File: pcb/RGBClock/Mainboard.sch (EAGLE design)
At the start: 88 parts, among them IC1 MCP23017SO, K1 G6K-2F, K2 G6K-2F, K3 G6K-2F, K4 G6K-2F, U1 71918-126LF, U10 NX3L1G384GW, U11 NX3L1G384GW, U12 NX3L1G384GW, U13 DRV612PW, U14 2N7002-7-F, U15 2N7002-7-F, U16 2N7002-7-F, U17 2N7002-7-F, U2 MAX6369KA+T, U3 TXS0102DCUR, U4 P82B96DR, U5 LM2675M-5.0, U6 DS1338Z-33+, U7 SI4735-D50, U8 TPS71533DCKR, U9 NX3L1G384GW, X2 5566-4, X3 1503_09, X4 1503_09, X5 5566-8

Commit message: 
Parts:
- removed U1: 71918-126LF, Fci:71918-126LF
- removed X2: 5566-4, con-molex:5566-4
- added CON1: (no value), con-harting:CON26
- added D11: CDSOD323-T03C, MyComponents:CDSOD323-T03C
- added X6: (no value), con-molex-micro-fit-3_0:HEADER_POS8_43045-0800
- X5: value 5566-8 -> (none); device con-molex:5566-8 -> con-molex-micro-fit-3_0:HEADER_POS4_43045-0401
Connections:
- removed net N$2: IC1.GPB3, U12.!E
- removed net N$32: IC1.GPB1, U10.!E
- removed net N$34: IC1.GPB2, U11.!E
- new net N$14: R2.1, U3.B1, U4.SX
- new net N$65: R3.1, U3.B2, U4.SY
- new net N$66: IC1.GPB1, U10.!E, U9.!E
- net +3V3: now also U7.!SEN
- net GND: now also CON1.6, D11.P$1, U7.RFGND, X5.1; no longer U1.6, X2-1.S
- net N$1: now also X5.2; no longer X2-2.S
- net N$12: now also X6.7; no longer X5-7.S
- net N$13: now also X6.8; no longer X5-8.S
- net N$20: now also X6.2; no longer X5-2.S
- net N$3: now also CON1.3; no longer U1.3
- net N$31: now also IC1.GPB2, U11.!E, U12.!E; no longer IC1.GPB0, U9.!E
- net N$33: now also IC1.GPB4; no longer IC1.GPB6
- net N$35: now also IC1.GPB3; no longer IC1.GPB4
- net N$38: now also IC1.GPB0; no longer IC1.GPB5
- net N$4: no longer R3.1, U3.B1, U4.SY
- net N$5: now also X6.1; no longer X5-1.S
- net N$52: now also X6.3; no longer X5-3.S
- net N$59: now also D11.P$2
- net N$6: now also CON1.5; no longer U1.5
- net N$60: now also X6.4; no longer X5-4.S
- net N$62: no longer R2.1, U3.B2, U4.SX
- net N$63: now also X6.5; no longer X5-5.S
- net N$64: now also X6.6; no longer X5-6.S
- net N$8: now also CON1.1; no longer U1.1
- net SCL_LONG: now also D3.KAT, R5.1, U4.RY, U4.TY, X5.4; no longer D2.KAT, R4.1, U4.RX, U4.TX, X2-3.S
- net SDA_LONG: now also D2.KAT, R4.1, U4.RX, U4.TX, X5.3; no longer D3.KAT, R5.1, U4.RY, U4.TY, X2-4.S
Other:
- note added: "3: SDA 4: SCL"
- note added: "SCL"
- note added: "SDA"

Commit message: 
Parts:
- D4: value (none) -> B130-13-F
- Q1, Q2: value (none) -> 32.768KHz
- R12: value (none) -> 100k
- R2, R3: value (none) -> 3k3
- X5: value (none) -> 43045-0400
- X6: value (none) -> 43045-0800
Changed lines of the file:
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@@
 <part name="U6" library="Maxim_By_element14_Batch_1" deviceset="DS1338Z-33+" device=""/>
 <part name="U14" library="Diodes" deviceset="2N7002-7-F" device=""/>
-<part name="R3" library="resistor" deviceset="R-EU_" device="0204/5"/>
-<part name="R2" library="resistor" deviceset="R-EU_" device="0204/5"/>
+<part name="R3" library="resistor" deviceset="R-EU_" device="0204/5" value="3k3"/>
+<part name="R2" library="resistor" deviceset="R-EU_" device="0204/5" value="3k3"/>
 <part name="U8" library="Texas" deviceset="TPS71533DCKR" device=""/>
 <part name="U5" library="Texas" deviceset="LM2675M-5.0" device=""/>
@@
 <part name="C2" library="rcl" deviceset="C-EU" device="C1206" value="4,7u"/>
 <part name="C1" library="rcl" deviceset="C-EU" device="C0805" value="100n"/>
-<part name="D4" library="diode" deviceset="DIODE-" device="DO-214AC"/>
+<part name="D4" library="diode" deviceset="DIODE-" device="DO-214AC" value="B130-13-F"/>
 <part name="GND1" library="supply1" deviceset="GND" device=""/>
 <part name="GND2" library="supply1" deviceset="GND" device=""/>
@@
 <part name="R15" library="resistor" deviceset="R-EU_" device="R0402" value="A2-0"/>
 <part name="GND34" library="supply1" deviceset="GND" device=""/>
-<part name="R12" library="resistor" deviceset="R-TRIMM" device="4G/J"/>
+<part name="R12" library="resistor" deviceset="R-TRIMM" device="4G/J" value="100k"/>
 <part name="GND36" library="supply1" deviceset="GND" device=""/>
 <part name="R4" library="resistor" deviceset="R-EU_" device="0204/2V" value="680R"/>
@@
 <part name="GND40" library="supply1" deviceset="GND" device=""/>
 <part name="+3V15" library="supply1" deviceset="+3V3" device=""/>
-<part name="Q1" library="crystal" deviceset="CRYSTAL" device="TC26V"/>
-<part name="Q2" library="crystal" deviceset="CRYSTAL" device="TC26V"/>
+<part name="Q1" library="crystal" deviceset="CRYSTAL" device="TC26V" value="32.768KHz"/>
+<part name="Q2" library="crystal" deviceset="CRYSTAL" device="TC26V" value="32.768KHz"/>
 <part name="IC1" library="Microchip" deviceset="MCP23017" device="SO"/>
 <part name="GND21" library="supply1" deviceset="GND" device=""/>
@@
 <part name="C4" library="MyComponents" deviceset="594D686X0010C2T" device=""/>
 <part name="L1" library="Bourns_By_element14_Batch_1" deviceset="SRR1240-680M" device=""/>
-<part name="X6" library="con-molex-micro-fit-3_0" deviceset="HEADER_POS8_?" device="43045-0800"/>
+<part name="X6" library="con-molex-micro-fit-3_0" deviceset="HEADER_POS8_?" device="43045-0800" value="43045-0800"/>
 <part name="D11" library="MyComponents" deviceset="CDSOD323-T03C" device=""/>
 <part name="GND14" library="supply1" deviceset="GND" device=""/>
 <part name="GND15" library="supply1" deviceset="GND" device=""/>
-<part name="X5" library="con-molex-micro-fit-3_0" deviceset="HEADER_POS4_?" device="43045-0401"/>
+<part name="X5" library="con-molex-micro-fit-3_0" deviceset="HEADER_POS4_?" device="43045-0401" value="43045-0400"/>
 <part name="CON1" library="con-harting" deviceset="CON26" device=""/>
 </parts>

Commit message: Cleanup schematic
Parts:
- removed U17: 2N7002-7-F, Diodes:2N7002-7-F
- removed X6: 43045-0800, con-molex-micro-fit-3_0:HEADER_POS8_43045-0800
- added U1: MAX6369KA+T, Maxim_By_element14_Batch_1:MAX6369KA+T
- added X2: 43045-0400, con-molex-micro-fit-3_0:HEADER_POS4_43045-0401
- D11: value CDSOD323-T03C -> 1N4148DO35-7; device MyComponents:CDSOD323-T03C -> diode:1N4148DO35-7
- D7: value 1N4148DO35-7 -> CDSOD323-T03C; device diode:1N4148DO35-7 -> MyComponents:CDSOD323-T03C
- U12: value NX3L1G384GW -> DRV612PW; device NXP_By_element14_Batch_1:NX3L1G384GW -> Texas:DRV612PW
- U13: value DRV612PW -> 2N7002-7-F; device Texas:DRV612PW -> Diodes:2N7002-7-F
- U2: value MAX6369KA+T -> TXS0102DCUR; device Maxim_By_element14_Batch_1:MAX6369KA+T -> Texas:TXS0102DCUR
- U3: value TXS0102DCUR -> P82B96DR; device Texas:TXS0102DCUR -> Texas:P82B96DR
- U4: value P82B96DR -> LM2675M-5.0; device Texas:P82B96DR -> Texas:LM2675M-5.0
- U5: value LM2675M-5.0 -> DS1338Z-33+; device Texas:LM2675M-5.0 -> Maxim_By_element14_Batch_1:DS1338Z-33+
- U6: value DS1338Z-33+ -> SI4735-D50; device Maxim_By_element14_Batch_1:DS1338Z-33+ -> SiliconLabs:SI4735-D50
- U7: value SI4735-D50 -> TPS71533DCKR; device SiliconLabs:SI4735-D50 -> Texas:TPS71533DCKR
- U8: value TPS71533DCKR -> NX3L1G384GW; device Texas:TPS71533DCKR -> NXP_By_element14_Batch_1:NX3L1G384GW
- X5: value 43045-0400 -> 43045-0800; device con-molex-micro-fit-3_0:HEADER_POS4_43045-0401 -> con-molex-micro-fit-3_0:HEADER_POS8_43045-0800
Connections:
- net +3V3: now also U1.SET0, U1.SET1, U1.SET2, U1.VCC, U12.VDD, U2.VCCB, U3.VCC, U5.VCC, U6.!SEN, U6.VA, U6.VD, U7.OUT, U8.VCC; no longer U12.VCC, U13.VDD, U2.SET0, U2.SET1, U2.SET2, U2.VCC, U3.VCCB, U4.VCC, U6.VCC, U7.!SEN, U7.VA, U7.VD, U8.OUT
- net +5V: now also U4.FB, U7.IN; no longer U5.FB, U8.IN
- net GND: now also D7.P$1, U1.GND, U12.GND_2, U13.S, U6.GND1, U6.GND2, U6.RFGND, U7.GND, X2.1; no longer D11.P$1, U13.GND, U13.GND_2, U17.S, U6.GND, U7.GND1, U7.GND2, U7.RFGND, X5.1
- net N$1: now also X2.2; no longer X5.2
- net N$10: now also U4.CB; no longer U5.CB
- net N$11: now also U4.VSW; no longer U5.VSW
- net N$12: now also X5.7; no longer X6.7
- net N$13: now also X5.8; no longer X6.8
- net N$14: now also U2.B1, U3.SX; no longer U3.B1, U4.SX
- net N$15: now also U5.X2; no longer U6.X2
- net N$16: now also U5.VBAT; no longer U6.VBAT
- net N$17: now also U5.X1; no longer U6.X1
- net N$18: now also U13.G; no longer U14.G
- net N$19: now also U14.G; no longer U15.G
- net N$20: now also X5.2; no longer X6.2
- net N$21: now also U15.G; no longer U16.G
- net N$22: now also D8.A, U13.D; no longer D7.A, U14.D
- net N$23: now also D9.A, U14.D; no longer D8.A, U15.D
- net N$24: now also D10.A, U15.D; no longer D9.A, U16.D
- net N$25: now also U6.GPO3/[DCLK]; no longer U7.GPO3/[DCLK]
- net N$26: now also U6.RCLK; no longer U7.RCLK
- net N$27: now also U6.LOUT/[DFS], U8.Y; no longer U7.LOUT/[DFS], U9.Y
- net N$28: now also U6.ROUT/[DOUT], U9.Y; no longer U10.Y, U7.ROUT/[DOUT]
- net N$29: now also U10.Z, U8.Z; no longer U11.Z, U9.Z
- net N$3: now also U2.A1; no longer U3.A1
- net N$30: now also U11.Z, U9.Z; no longer U10.Z, U12.Z
- net N$31: now also U10.!E; no longer U12.!E
- net N$33: now also U1.WDI; no longer U2.WDI
- net N$35: now also U6.!RST; no longer U7.!RST
- net N$36: now also D7.P$2, U11.Y; no longer D6.P$2, U12.Y
- net N$37: now also D6.P$2, U10.Y; no longer D5.P$2, U11.Y
- net N$38: now also U12.~MUTE; no longer U13.~MUTE
- net N$4: now also U5.SDA, U6.SDIO; no longer U6.SDA, U7.SDIO
- net N$40: now also U12.OUT_L; no longer U13.OUT_L
- net N$44: now also U12.OUT_R; no longer U13.OUT_R
- net N$46: now also U12.GAIN; no longer U13.GAIN
- net N$5: now also X5.1; no longer X6.1
- net N$51: now also U1.~WDO; no longer U2.~WDO
- net N$52: now also X5.3; no longer X6.3
- net N$53: now also U12.-IN_L; no longer U13.-IN_L
- net N$54: now also U12.CP; no longer U13.CP
- net N$55: now also U12.-IN_R; no longer U13.-IN_R
- net N$56: now also U12.CN; no longer U13.CN
- net N$57: now also U12.VSS; no longer U13.VSS
- net N$59: now also D5.P$2, U6.FMI; no longer D11.P$2, U7.FMI
- net N$6: now also U2.A2; no longer U3.A2
- net N$60: now also X5.4; no longer X6.4
- net N$61: now also U6.DBYP; no longer U7.DBYP
- net N$62: now also U5.SCL, U6.SCLK; no longer U6.SCL, U7.SCLK
- net N$63: now also X5.5; no longer X6.5
- net N$64: now also X5.6; no longer X6.6
- net N$65: now also U2.B2, U3.SY; no longer U3.B2, U4.SY
- net N$66: now also U8.!E; no longer U10.!E
- net N$7: now also U16.G; no longer U17.G
- net N$8: now also U2.OE, U2.VCCA; no longer U3.OE, U3.VCCA
- net N$9: now also D11.A, U16.D; no longer D10.A, U17.D
- net SCL_LONG: now also U3.RY, U3.TY, X2.4; no longer U4.RY, U4.TY, X5.4
- net SDA_LONG: now also U3.RX, U3.TX, X2.3; no longer U4.RX, U4.TX, X5.3
- net VCC: now also D11.C, U4.VIN; no longer D7.C, U5.VIN
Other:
- moved on the sheet: D10, D5, D6, D8, D9, JP1, U10, U11, U14, U15, U16, U2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

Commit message: Beta version master pcb (not complete routed !)
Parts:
- renumbered TP1 to ANT
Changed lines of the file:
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@@
 <part name="C10" library="rcl" deviceset="C-EU" device="C1005" value="22p"/>
 <part name="C5" library="rcl" deviceset="C-EU" device="C1005" value="1n"/>
-<part name="TP1" library="testpad" deviceset="PTR1" device="PAD1-13"/>
+<part name="ANT" library="testpad" deviceset="PTR1" device="PAD1-13"/>
 <part name="C12" library="rcl" deviceset="C-EU" device="C1005" value="22n"/>
 <part name="+3V16" library="supply1" deviceset="+3V3" device=""/>
@@
 <instance part="C10" gate="G$1" x="149.86" y="43.18" rot="R180"/>
 <instance part="C5" gate="G$1" x="101.6" y="76.2"/>
-<instance part="TP1" gate="G$1" x="101.6" y="86.36" rot="R180"/>
+<instance part="ANT" gate="G$1" x="101.6" y="86.36" rot="R180"/>
 <instance part="C12" gate="G$1" x="165.1" y="83.82" smashed="yes" rot="R270">
 <attribute name="NAME" x="169.164" y="81.661" size="1.778" layer="95"/>
@@
 <net name="N$58" class="0">
 <segment>
-<pinref part="TP1" gate="G$1" pin="TP"/>
+<pinref part="ANT" gate="G$1" pin="TP"/>
 <pinref part="C5" gate="G$1" pin="1"/>
 <wire x1="101.6" y1="83.82" x2="101.6" y2="78.74" width="0.1524" layer="91"/>

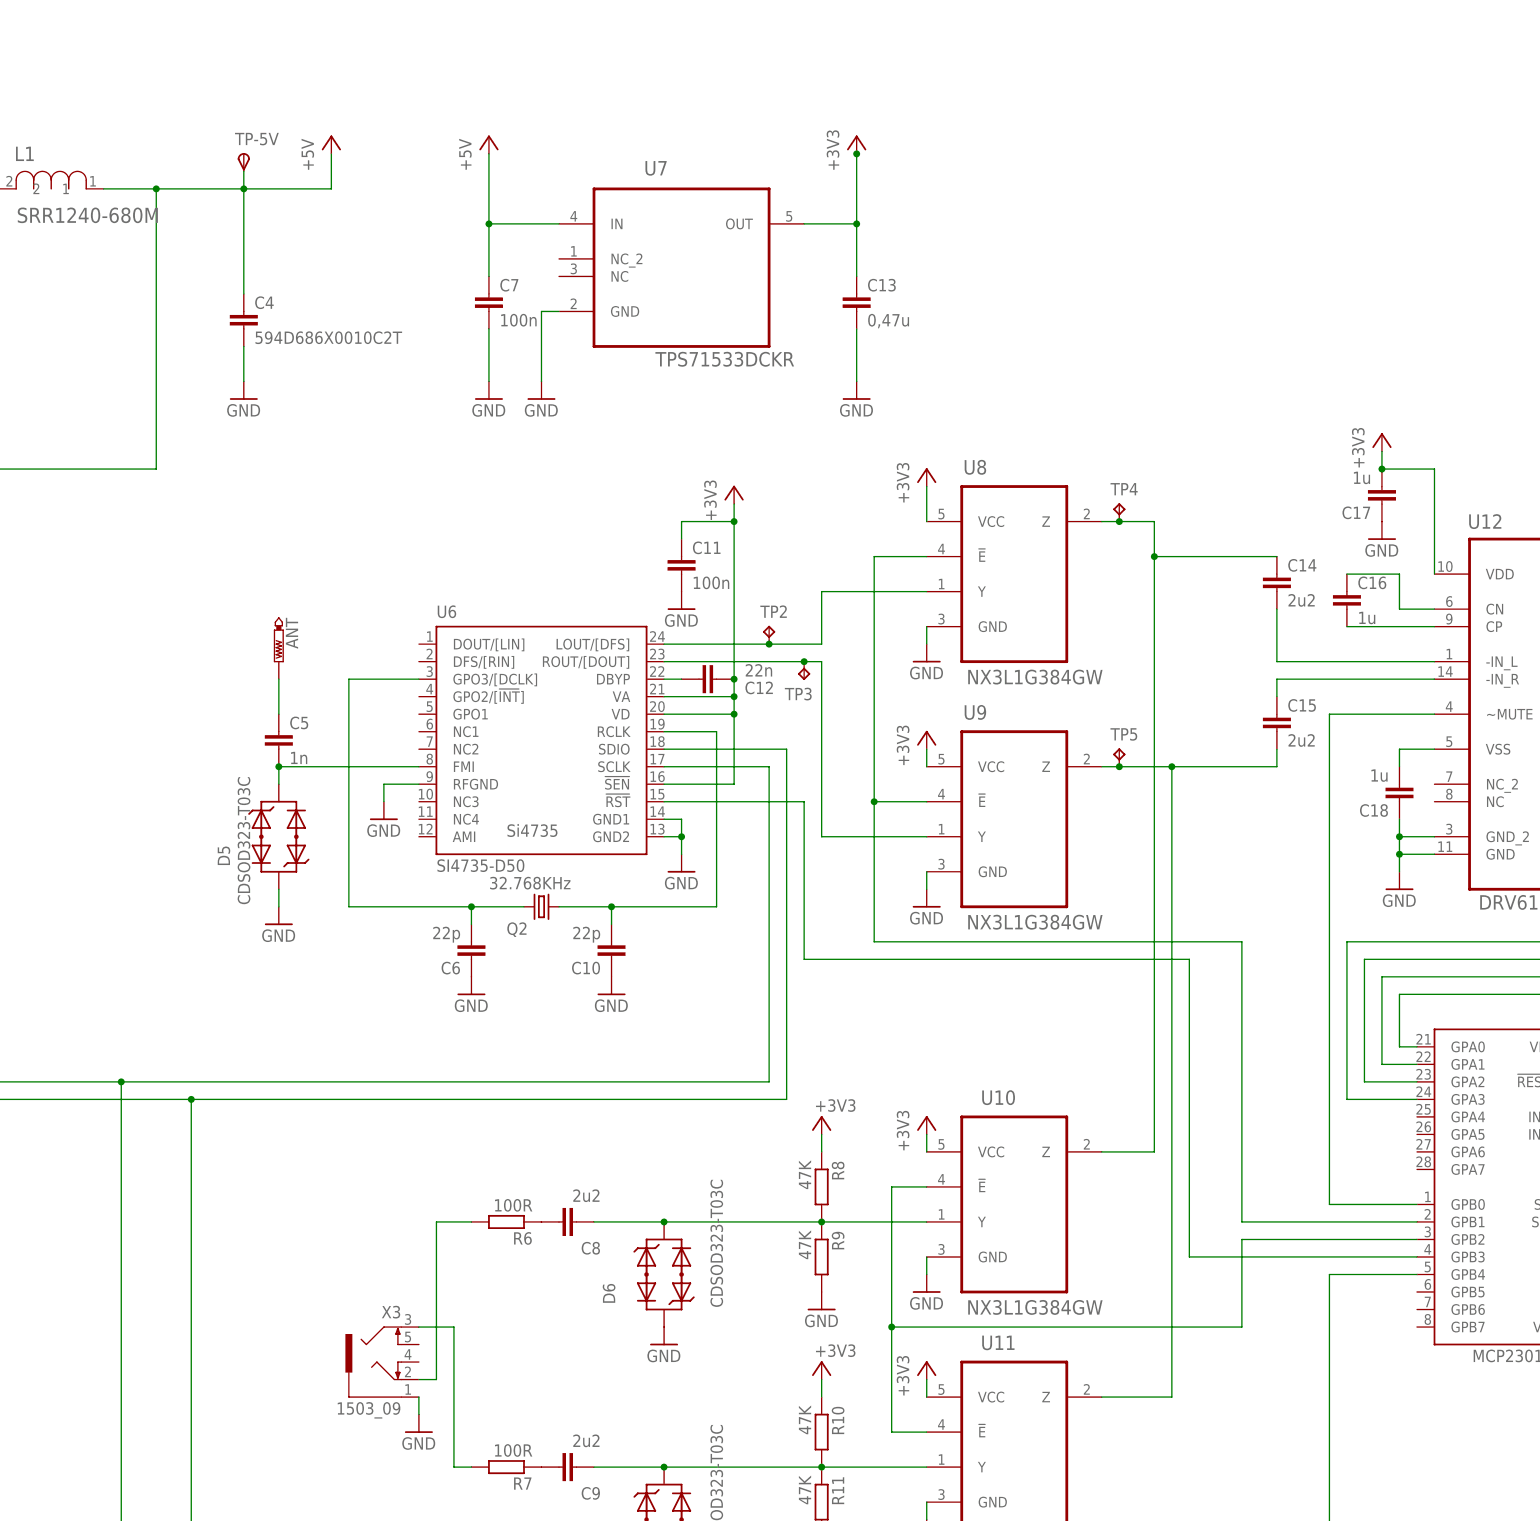
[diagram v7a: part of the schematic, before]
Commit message: Adding analog power and light sensor
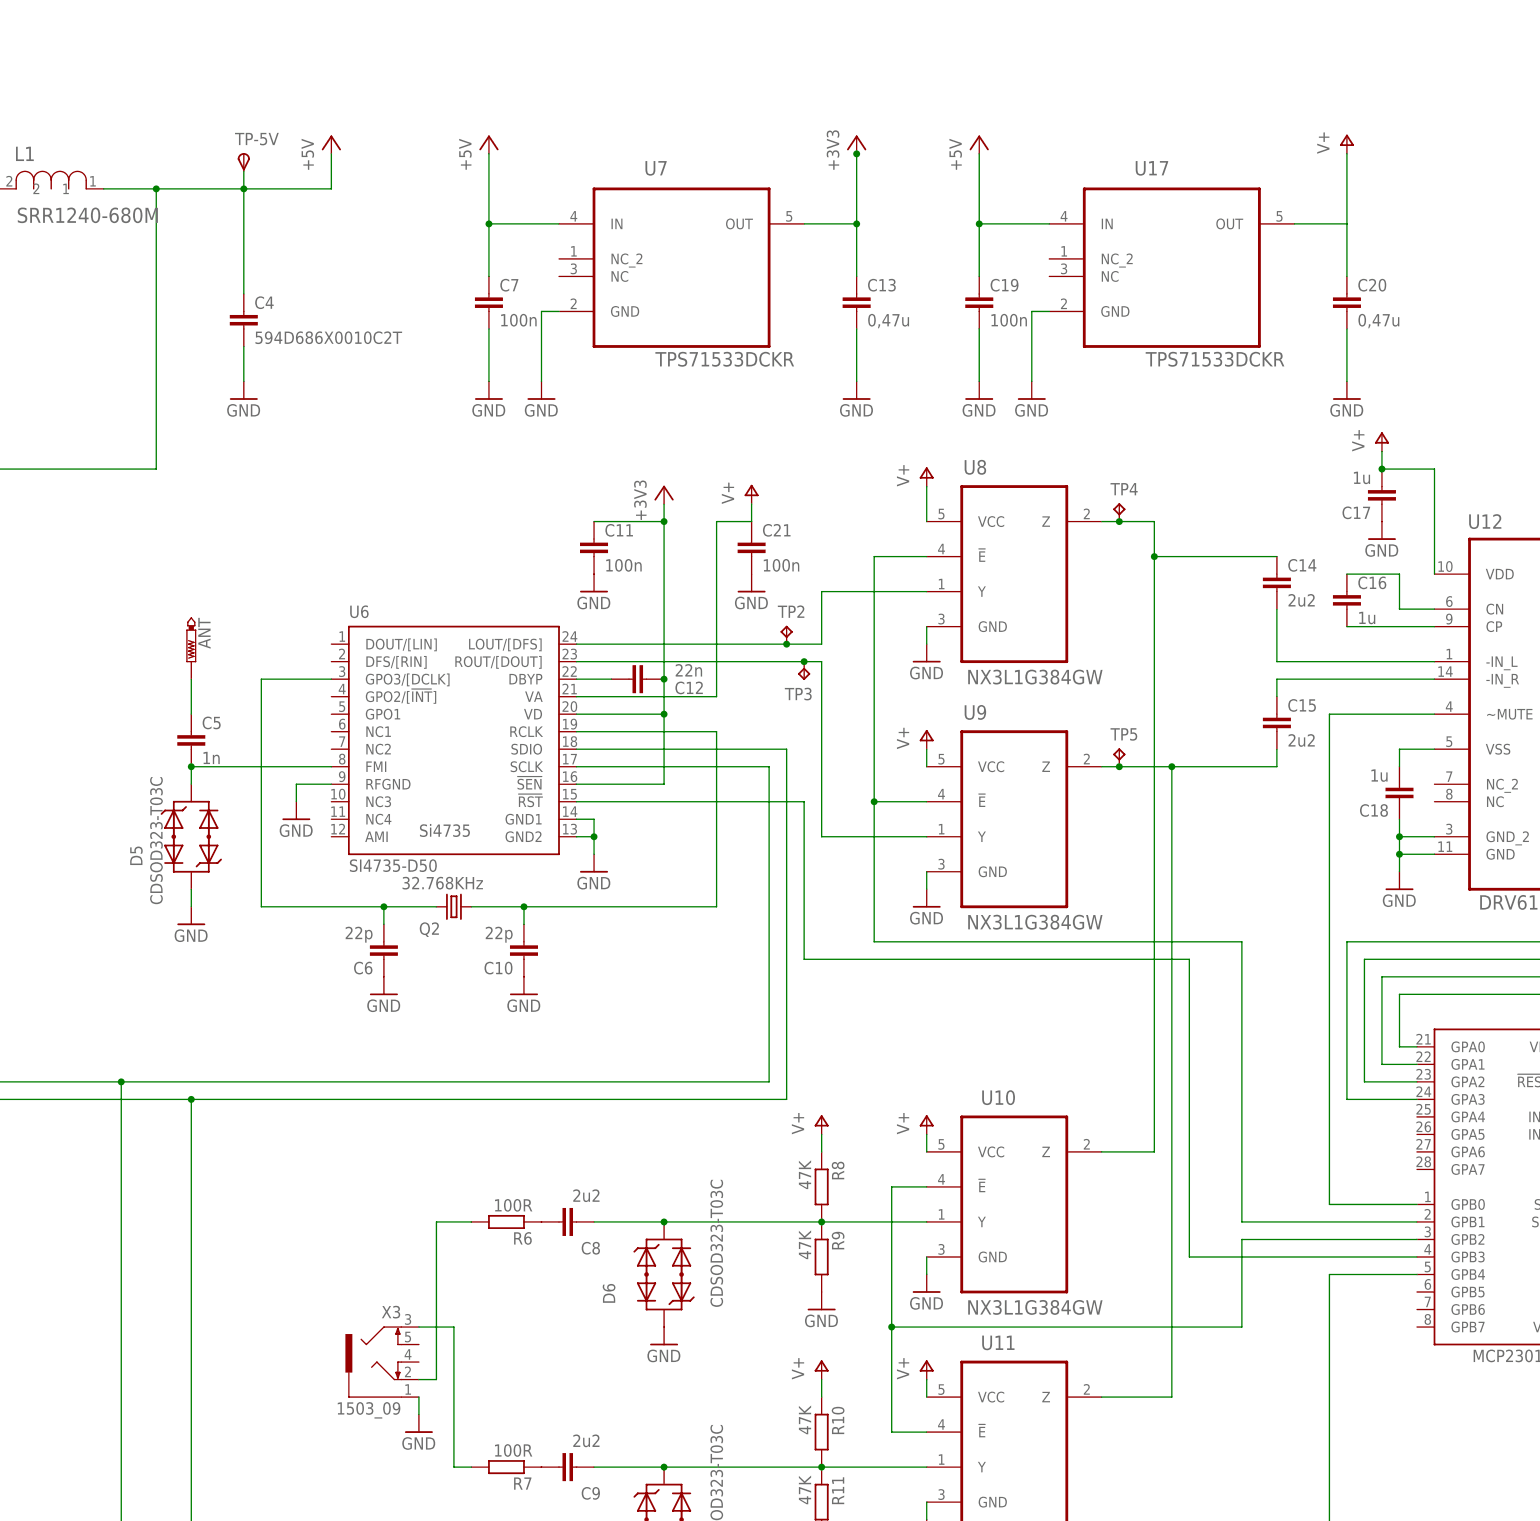
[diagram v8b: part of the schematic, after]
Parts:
- added C19: 100n, rcl:C-EUC0805
- added C20: 0,47u, rcl:C-EUC1206
- added C21: 100n, rcl:C-EUC1005
- added U17: TPS71533DCKR, Texas:TPS71533DCKR
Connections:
- new net 3V3A: C17.2, C20.1, C21.1, R10.1, R8.1, U10.VCC, U11.VCC, U12.VDD, U17.OUT, U6.VA, U8.VCC, U9.VCC
- net +3V3: no longer C17.2, R10.1, R8.1, U10.VCC, U11.VCC, U12.VDD, U6.VA, U8.VCC, U9.VCC
- net +5V: now also C19.1, U17.IN
- net GND: now also C19.2, C20.2, C21.2, U17.GND
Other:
- moved on the sheet: ANT, C10, C11, C12, C5, C6, D5, Q2, TP2, U6
